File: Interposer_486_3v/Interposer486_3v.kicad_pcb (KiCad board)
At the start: 2 copper layers, 48.3 x 81.9 mm, 243 parts, among them J1 WB/~WT, J2 CLKMUL, J3 V Select, U1 LT1085-ADJ

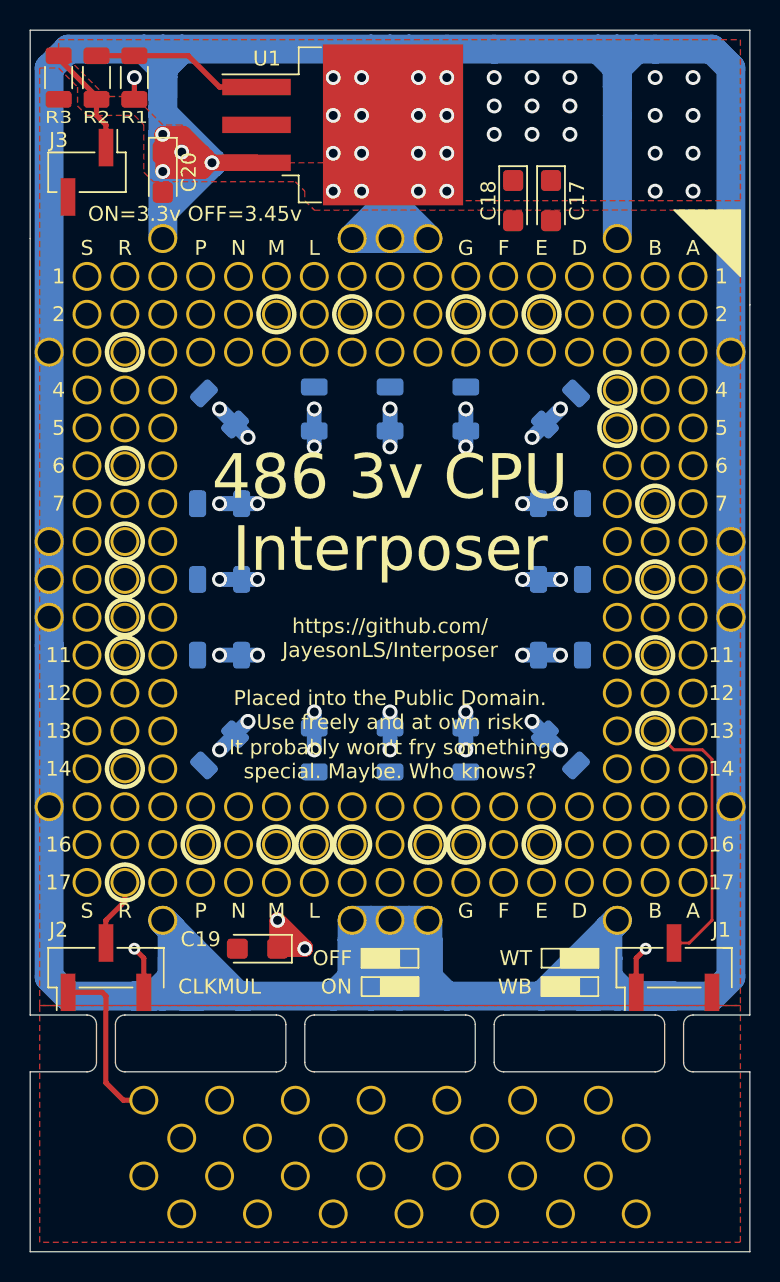
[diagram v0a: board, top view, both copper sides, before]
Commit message: Rename Interposer_486_3v folder.
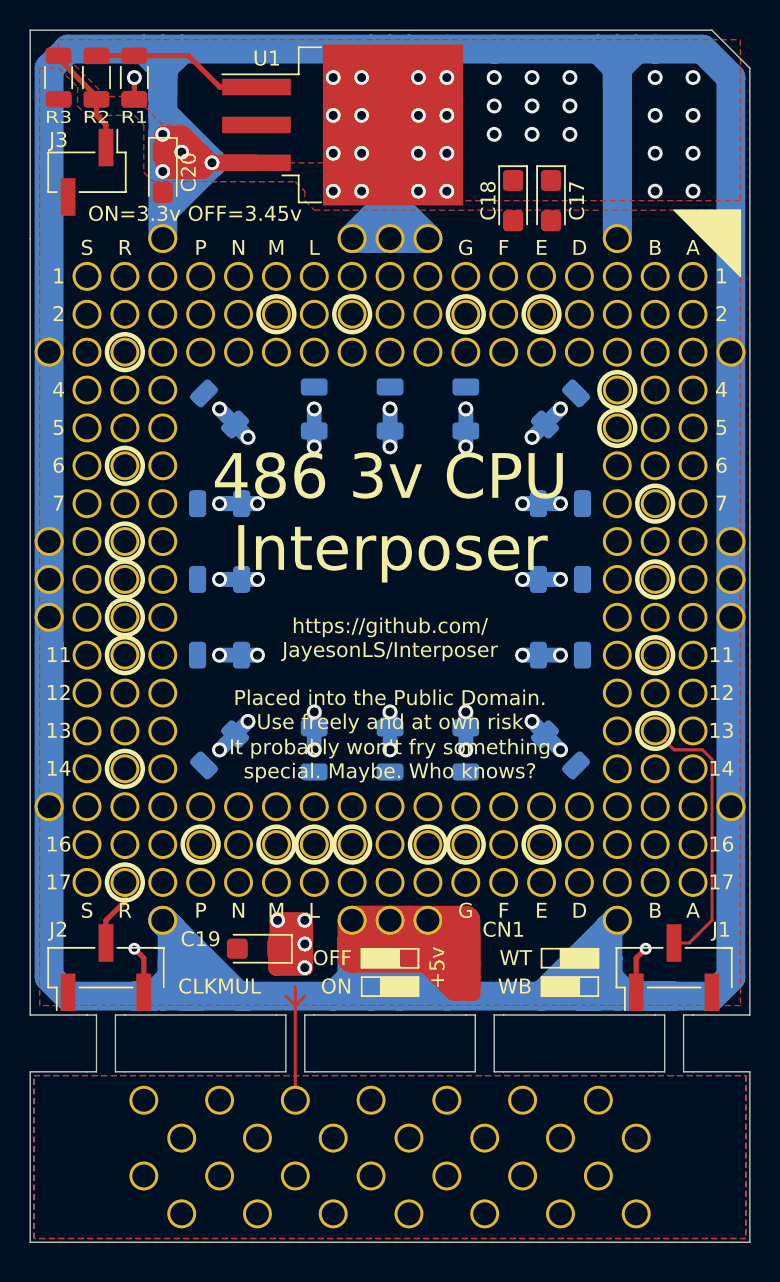
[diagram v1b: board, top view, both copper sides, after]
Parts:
- added CN1: +5v External, Connector_Wire:SolderWirePad_1x01_SMD_1x2mm, F.Cu at (162.6, 107.7)
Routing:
- net +5V: track 408.2 -> 447.7 mm
- net VCC: track 14.1 -> 25.4 mm, vias 38 -> 40
- net VSS: track 52.7 -> 50.8 mm
- added copper zone on B.Cu, net VSS
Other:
- board size 48.3 x 81.9 mm -> 48.3 x 81.3 mm
- board text added: "+5v"
